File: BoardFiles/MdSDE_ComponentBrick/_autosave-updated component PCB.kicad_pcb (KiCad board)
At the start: 2 copper layers, 96.5 x 47 mm, 42 parts, among them P101 CONN_01X10, P102 CONN_01X10, SW202 SPST_x3, SW302 SPST_x3, SW402 SPST_x3, SW502 SPST_x3, SW602 SPST_x3, SW702 SPST_x3, SW802 SPST_x3, SW902 SPST_x3

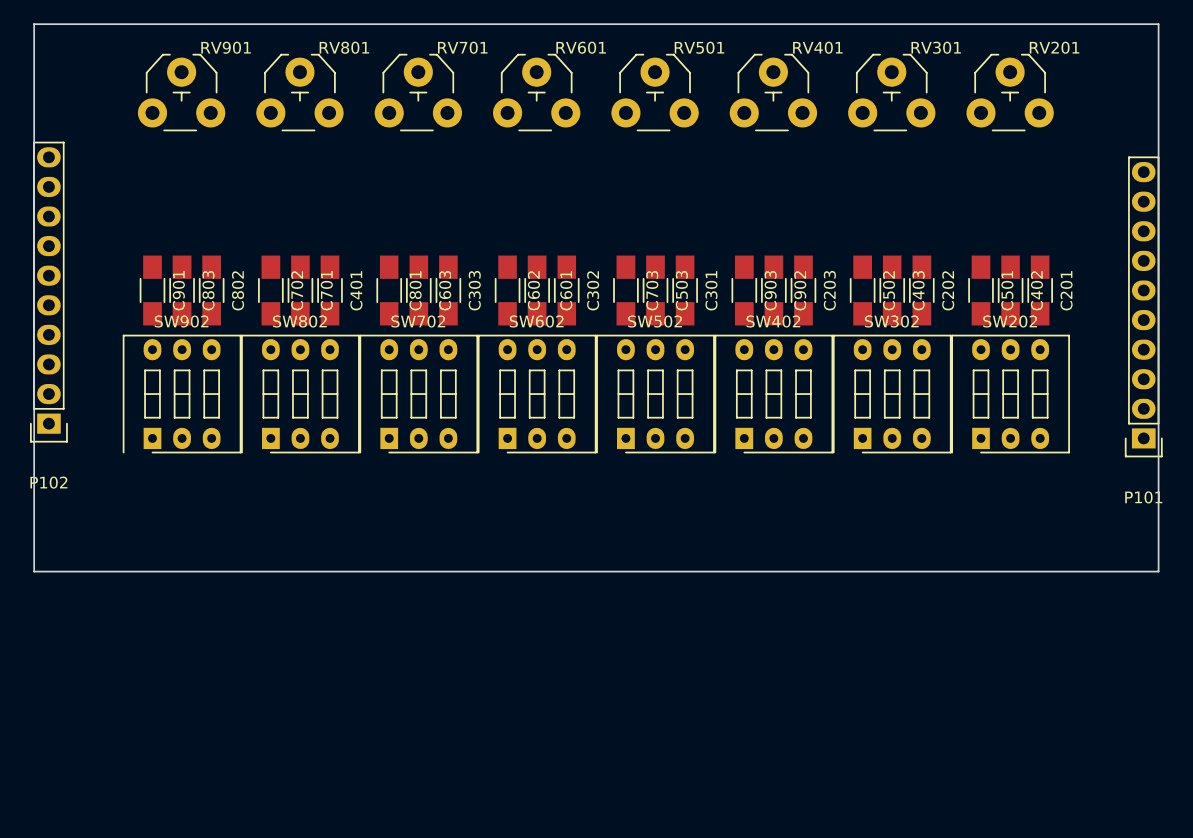
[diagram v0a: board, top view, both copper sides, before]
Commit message: Updated footprints
Reduced size of bounding rectangle on components
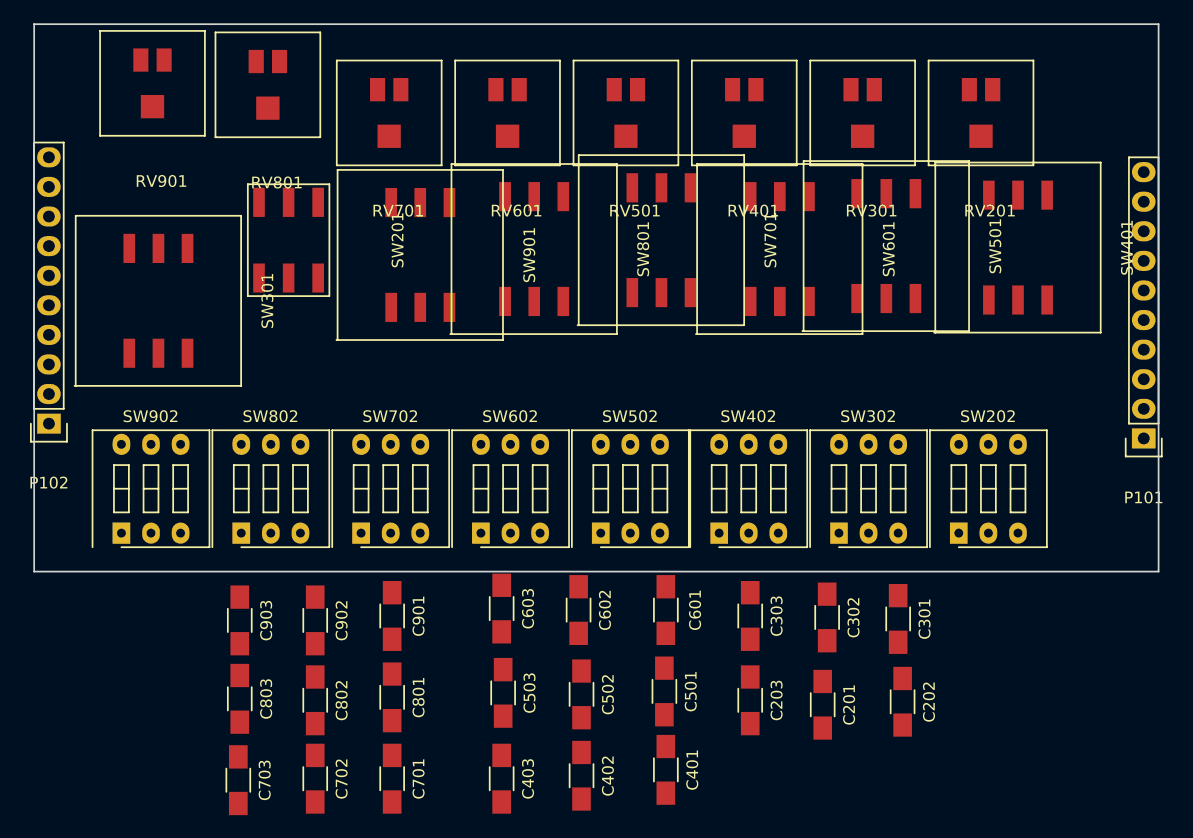
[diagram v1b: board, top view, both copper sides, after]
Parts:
- added SW201: Coded_Switch, SH-7000RotarySwitch, F.Cu at (75.2, 84.6)
- added SW301: Coded_Switch, Footprints:SH-7000RotarySwitch, F.Cu at (64.0, 89.8)
- added SW401: Coded_Switch, Footprints:SH-7000RotarySwitch, F.Cu at (137.8, 85.2)
- added SW501: Coded_Switch, Footprints:SH-7000RotarySwitch, F.Cu at (126.5, 85.1)
- added SW601: Coded_Switch, Footprints:SH-7000RotarySwitch, F.Cu at (117.3, 85.3)
- added SW701: Coded_Switch, Footprints:SH-7000RotarySwitch, F.Cu at (107.2, 84.6)
- added SW801: Coded_Switch, Footprints:SH-7000RotarySwitch, F.Cu at (96.3, 85.3)
- added SW901: Coded_Switch, Footprints:SH-7000RotarySwitch, F.Cu at (86.5, 85.9)
- RV201, RV301, RV401, RV501, RV601, RV701, RV801, RV901: footprint Potentiometers:Potentiometer_VishaySpectrol-Econtrim-Type36P -> Footprints:3314_Potentiometer
- moved C402 55.6 mm to (100.3, 130.6)
- moved C403 53.7 mm to (93.5, 130.8)
- moved C703 53.6 mm to (70.9, 130.9)
- moved C903 51.7 mm to (71.0, 117.2)
- moved C401 50.2 mm to (107.6, 130.0)
- moved C902 48.5 mm to (77.5, 117.2)
- moved C501 43.9 mm to (107.4, 123.3)
- moved C701 42.6 mm to (84.1, 130.8)
- moved C502 42.2 mm to (100.3, 123.6)
- moved C702 42.1 mm to (77.5, 130.8)
- moved C201 40.2 mm to (121.0, 124.5)
- moved C303 38.1 mm to (114.8, 116.8)
- moved C503 36.9 mm to (93.6, 123.4)
- moved C802 36.3 mm to (77.5, 124.1)
- moved C302 35.9 mm to (121.4, 117.0)
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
